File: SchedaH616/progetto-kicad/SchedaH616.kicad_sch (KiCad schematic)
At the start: 0 parts

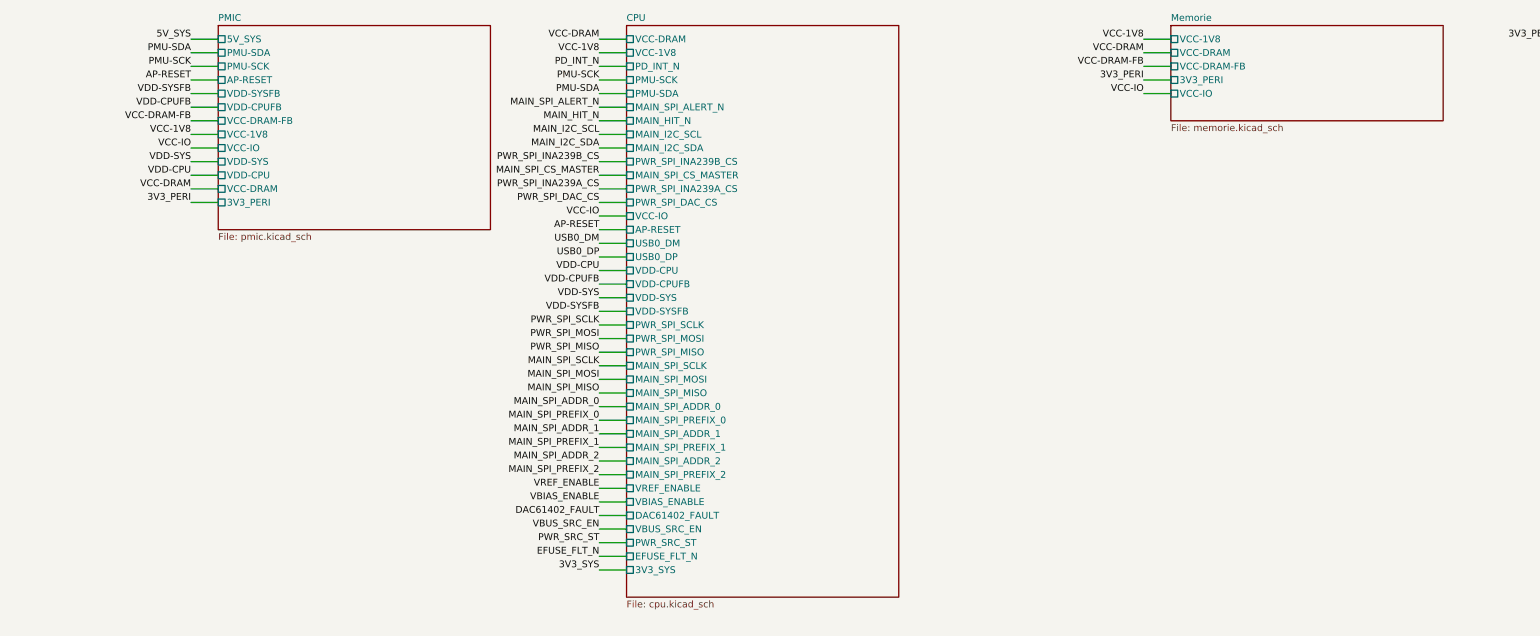
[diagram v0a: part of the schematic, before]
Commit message: SchedaH616: placement PCB 50x70 a 6 strati e modifiche allo schema
PCB (solo placement, niente piste), generato da generatori/build_pcb.sh:
- 50 x 70 mm, smussi 3 mm, 4 fori NPTH 2.2 mm con keepout, 6 strati
- H616 al centro, LPDDR4 sul lato DRAM, AXP313A vicino alla CPU, eMMC vicino ai pin PC
- connettori sui bordi, U.FL Wi-Fi e SMA GNSS su lati opposti
- disaccoppiamento di H616 e LPDDR4 sul bottom sotto le sfere
- regole: piste 5 mil, via-in-pad 0.25/0.15 sotto l'H616
- DRC: 0 violazioni (solo collegamenti da fare), parità schema/PCB ok

Schema (modifiche approvate):
- LPDDR4 confermata come scelta definitiva
- USB host di nuovo su USB-C solo host (Rp 22k, USBLC6-2, TPS2553)
- jack 5 V diretto su IN1 del TPS2121, tolto l'SS54, TPS56637 in Eco-mode
- LDO AP2112K-1.8 (C176944) dedicato a VCCQ eMMC e VCC_PC
- ERC 0

Libreria H616.pretty: serigrafia sui pad tolta, pioli di centraggio NPTH.

Co-Authored-By: Claude Opus 5.5 (1M context) <noreply@anthropic.com>
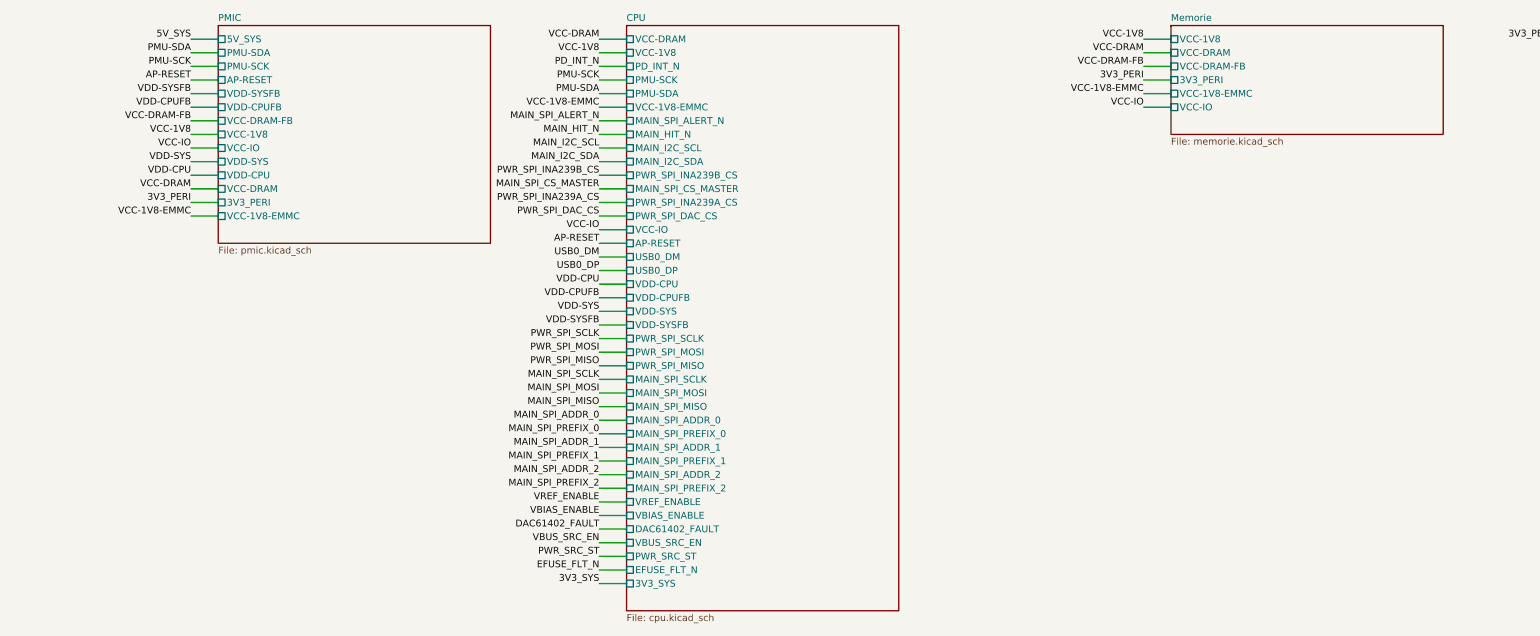
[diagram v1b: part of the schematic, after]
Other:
- sheet CPU ports: added VCC-1V8-EMMC; removed none
- sheet Memorie ports: added VCC-1V8-EMMC; removed none
- sheet PMIC ports: added VCC-1V8-EMMC; removed none

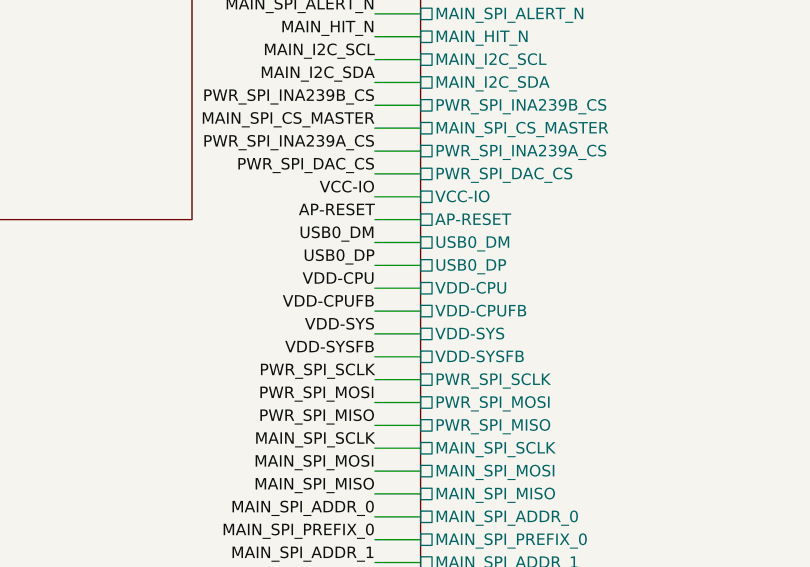
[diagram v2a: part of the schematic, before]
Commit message: SchedaH616: verifica sullo schema Orange Pi Zero3 (LPDDR4, AXP313A, reset)
- Mappa CA/CS/CK/CKE/RESET della LPDDR4 verificata 8/8 sulla Zero3, sfere della LPDDR4, ODT 100k e ZQ 240R coincidono
- AXP313A allineato alla Zero3: 22 uF sui VIN, 2x47 uF + 1 uF + 100 nF sulle uscite DCDC, DLDO1 47 uF, RTCLDO 4.7 uF, PWRON 100 nF montato
- DCDC3 a 1.1 V impostato dall'SPL di U-Boot (CONFIG_AXP_DCDC3_VOLT)
- RESET H616: 10k a VCC-1V8, 1 nF, 100R in serie da AP-RESET; AC_AVCC 10 uF; quarzo 24 MHz con 12 pF
- scelte-progetto.md: verifiche segnate, differenze volute (VCC_PG 3.3 V, VCC_PC 1.8 V), nuovo punto aperto sugli strap BOOT_SEL
- ERC 0, parita' 0, DRC 0 (solo collegamenti da fare)

Co-Authored-By: Claude Opus 5.5 (1M context) <noreply@anthropic.com>
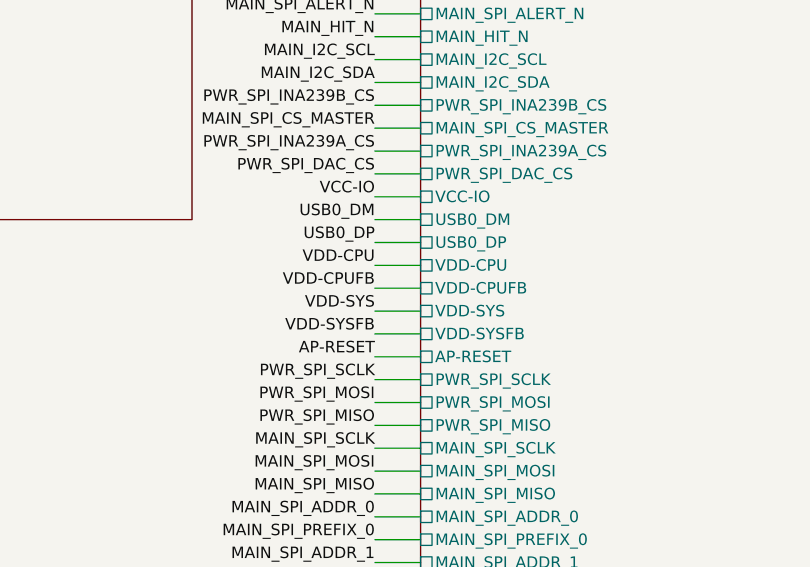
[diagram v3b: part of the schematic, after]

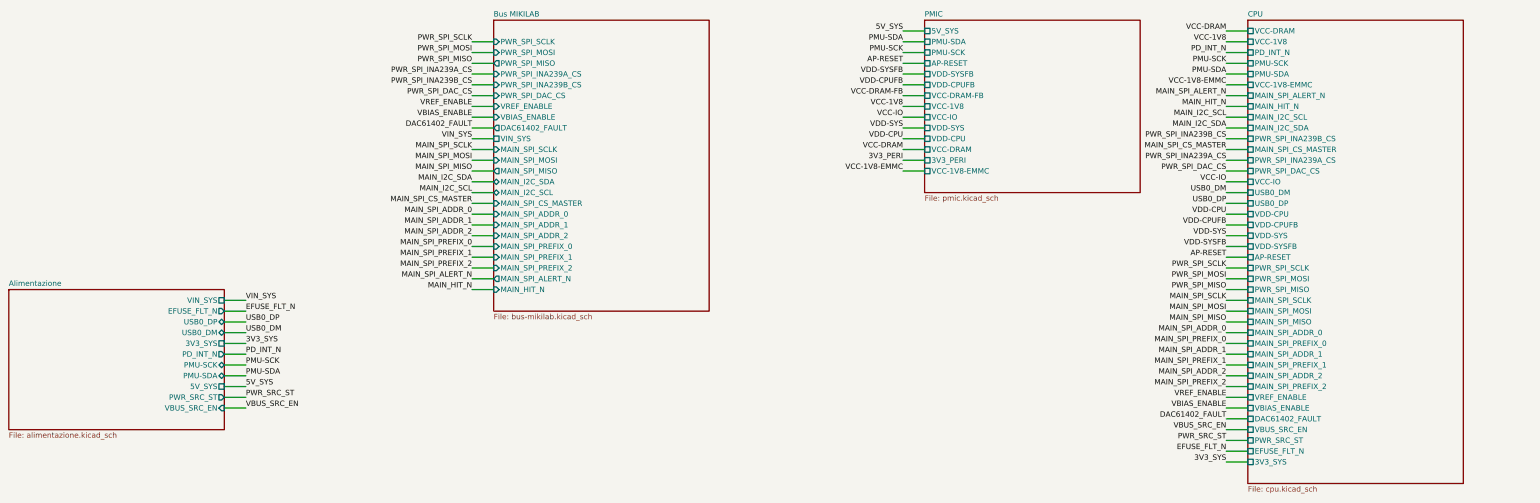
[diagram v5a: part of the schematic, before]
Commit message: SchedaH616: eFuse TPS259470 eliminato
- tolti U106 TPS259470 e i suoi componenti (partitore UVLO/OVLO, RILM, dVdT, 1 uF d'ingresso) e il footprint RPW dalla libreria
- VIN_SYS dal BUS_POWER direttamente all'ingresso del TPS56637 (restano C101/C102 10 uF e C125 100 nF)
- ingresso 12 V senza limite di corrente, OVP ne' blocco inverso; nessuna TVS sui 12 V
- P17 del TCA6416A ora libera; documenti aggiornati
- ERC 0, parita' 0, DRC 0 (solo collegamenti da fare)

Co-Authored-By: Claude Opus 5.5 (1M context) <noreply@anthropic.com>
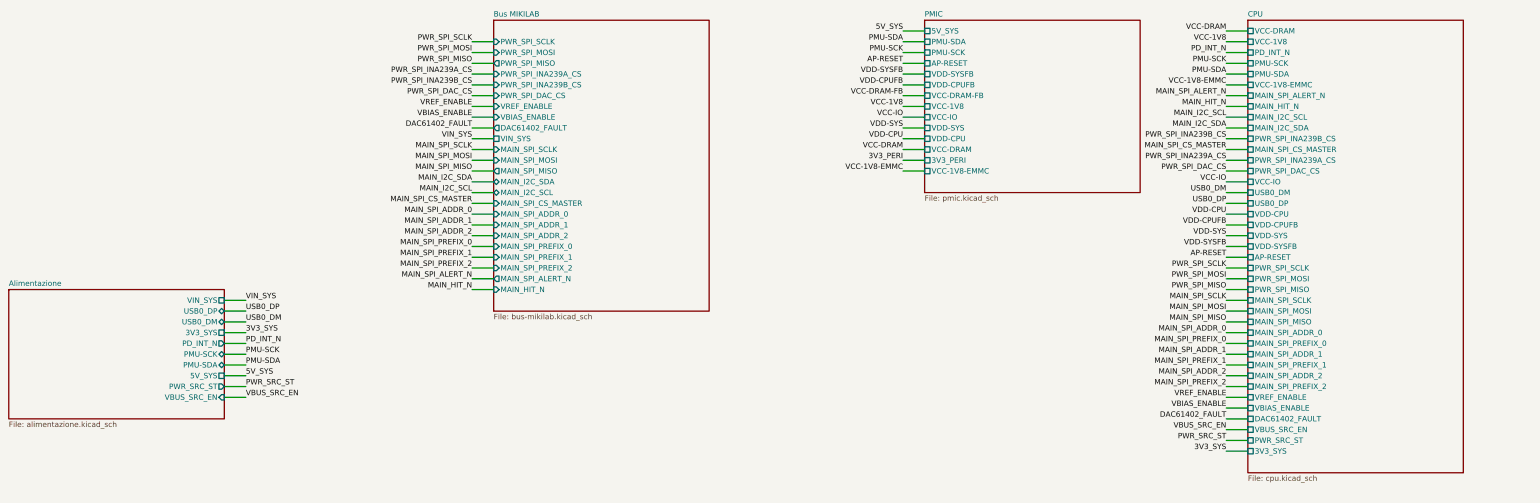
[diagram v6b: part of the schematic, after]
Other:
- sheet Alimentazione ports: added none; removed EFUSE_FLT_N
- sheet CPU ports: added none; removed EFUSE_FLT_N
